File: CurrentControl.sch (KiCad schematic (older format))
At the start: 7 parts

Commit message: Initial annotation
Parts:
- Q201: renamed from Q?; footprint (none) -> Transistors_TO-220:TO-220_FET-GDS_Vertical
- R201, R202: renamed from R?; footprint (none) -> Resistors_SMD:R_0603_HandSoldering
- R203: renamed from R?; footprint (none) -> Resistors_ThroughHole:Resistor_Vertical_RM5mm
- U201: renamed from U?; footprint (none) -> SMD_Packages:SSOP-8
- gave numbers to parts that had none: 2
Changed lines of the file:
@@
 $EndDescr
 $Comp
-L R R?
+L R R202
 U 1 1 54E39380
 P 3200 3800
-F 0 "R?" V 3280 3800 50  0000 C CNN
+F 0 "R202" V 3280 3800 50  0000 C CNN
 F 1 "R" V 3207 3801 50  0000 C CNN
-F 2 "" V 3130 3800 30  0000 C CNN
+F 2 "Resistors_SMD:R_0603_HandSoldering" V 3130 3800 30  0001 C CNN
 F 3 "" H 3200 3800 30  0000 C CNN
 	1    3200 3800
@@
 $EndComp
 $Comp
-L R R?
+L R R203
 U 1 1 54E39388
 P 6650 4350
-F 0 "R?" V 6730 4350 50  0000 C CNN
+F 0 "R203" V 6730 4350 50  0000 C CNN
 F 1 ".1" V 6657 4351 50  0000 C CNN
-F 2 "" V 6580 4350 30  0000 C CNN
+F 2 "Resistors_ThroughHole:Resistor_Vertical_RM5mm" V 6580 4350 30  0001 C CNN
 F 3 "" H 6650 4350 30  0000 C CNN
 F 4 "AC01000001007JA100" V 6650 4350 60  0001 C CNN "MPN"
@@
 $EndComp
 $Comp
-L LMV358 U?
+L LMV358 U201
 U 1 1 54E3939B
 P 4550 3000
-F 0 "U?" H 4500 3200 60  0000 L CNN
+F 0 "U201" H 4500 3200 60  0000 L CNN
 F 1 "LMV358" H 4500 2750 60  0000 L CNN
-F 2 "" H 4550 3000 60  0000 C CNN
+F 2 "SMD_Packages:SSOP-8" H 4550 3000 60  0001 C CNN
 F 3 "" H 4550 3000 60  0000 C CNN
 	1    4550 3000
@@
 $EndComp
 $Comp
-L MOSFET_N Q?
+L MOSFET_N Q201
 U 1 1 54E393A3
 P 6550 3000
-F 0 "Q?" H 6560 3170 50  0000 R CNN
+F 0 "Q201" H 6560 3170 50  0000 R CNN
 F 1 "BUK9575" H 6500 2850 50  0000 R CNN
-F 2 "" H 6550 3000 60  0000 C CNN
+F 2 "Transistors_TO-220:TO-220_FET-GDS_Vertical" H 6550 3000 60  0001 C CNN
 F 3 "" H 6550 3000 60  0000 C CNN
 F 4 "BUK9575-100A,127" H 6550 3000 60  0001 C CNN "MPN"
@@
 $EndComp
 $Comp
-L C C?
+L C C201
 U 1 1 54E393B0
 P 4050 2300
-F 0 "C?" H 4100 2400 50  0000 L CNN
+F 0 "C201" H 4100 2400 50  0000 L CNN
 F 1 "C" H 4100 2200 50  0000 L CNN
-F 2 "" H 4088 2150 30  0000 C CNN
+F 2 "" H 4088 2150 30  0001 C CNN
 F 3 "" H 4050 2300 60  0000 C CNN
 	1    4050 2300
@@
 	3850 3100 3850 3950
 $Comp
-L POT RV?
+L POT RV201
 U 1 1 54E393C3
 P 3200 3100
-F 0 "RV?" H 3200 3000 50  0000 C CNN
+F 0 "RV201" H 3200 3000 50  0000 C CNN
 F 1 "POT" H 3200 3100 50  0000 C CNN
-F 2 "" H 3200 3100 60  0000 C CNN
+F 2 "" H 3200 3100 60  0001 C CNN
 F 3 "" H 3200 3100 60  0000 C CNN
 	1    3200 3100
@@
 	6650 2000 6650 2800
 $Comp
-L R R?
+L R R201
 U 1 1 54E39622
 P 5650 3000
-F 0 "R?" V 5730 3000 50  0000 C CNN
+F 0 "R201" V 5730 3000 50  0000 C CNN
 F 1 "1K" V 5657 3001 50  0000 C CNN
-F 2 "" V 5580 3000 30  0000 C CNN
+F 2 "Resistors_SMD:R_0603_HandSoldering" V 5580 3000 30  0001 C CNN
 F 3 "" H 5650 3000 30  0000 C CNN
 	1    5650 3000

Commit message: Preliminary footprint association
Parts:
- C201: footprint (none) -> SMD_Packages:SMD-0805
- R201, R202: footprint Resistors_SMD:R_0603_HandSoldering -> SMD_Packages:SMD-0805
- R203: footprint Resistors_ThroughHole:Resistor_Vertical_RM5mm -> Resistors_ThroughHole:Resistor_Horizontal_RM15mm
- RV201: footprint (none) -> Potentiometers:Potentiometer_WirePads_largePads
- U201: footprint SMD_Packages:SSOP-8 -> SMD_Packages:SOIC-8-N; MPN (none) -> LMV358IDT
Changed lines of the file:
@@
 F 0 "R202" V 3280 3800 50  0000 C CNN
 F 1 "R" V 3207 3801 50  0000 C CNN
-F 2 "Resistors_SMD:R_0603_HandSoldering" V 3130 3800 30  0001 C CNN
+F 2 "SMD_Packages:SMD-0805" V 3130 3800 30  0001 C CNN
 F 3 "" H 3200 3800 30  0000 C CNN
 	1    3200 3800
@@
 F 0 "R203" V 6730 4350 50  0000 C CNN
 F 1 ".1" V 6657 4351 50  0000 C CNN
-F 2 "Resistors_ThroughHole:Resistor_Vertical_RM5mm" V 6580 4350 30  0001 C CNN
+F 2 "Resistors_ThroughHole:Resistor_Horizontal_RM15mm" V 6580 4350 30  0001 C CNN
 F 3 "" H 6650 4350 30  0000 C CNN
 F 4 "AC01000001007JA100" V 6650 4350 60  0001 C CNN "MPN"
@@
 F 0 "U201" H 4500 3200 60  0000 L CNN
 F 1 "LMV358" H 4500 2750 60  0000 L CNN
-F 2 "SMD_Packages:SSOP-8" H 4550 3000 60  0001 C CNN
-F 3 "" H 4550 3000 60  0000 C CNN
+F 2 "SMD_Packages:SOIC-8-N" H 4550 3000 60  0001 C CNN
+F 3 "http://www.produktinfo.conrad.com/datenblaetter/1100000-1199999/001185383-da-01-en-IC_OP_AMP_DUAL_R_R_LMV358IDT_SOIC_8_STM.pdf" H 4550 3000 60  0001 C CNN
+F 4 "LMV358IDT" H 4550 3000 60  0001 C CNN "MPN"
 	1    4550 3000
 	1    0    0    -1
@@
 F 0 "C201" H 4100 2400 50  0000 L CNN
 F 1 "C" H 4100 2200 50  0000 L CNN
-F 2 "" H 4088 2150 30  0001 C CNN
+F 2 "SMD_Packages:SMD-0805" H 4088 2150 30  0001 C CNN
 F 3 "" H 4050 2300 60  0000 C CNN
 	1    4050 2300
@@
 F 0 "RV201" H 3200 3000 50  0000 C CNN
 F 1 "POT" H 3200 3100 50  0000 C CNN
-F 2 "" H 3200 3100 60  0001 C CNN
+F 2 "Potentiometers:Potentiometer_WirePads_largePads" H 3200 3100 60  0001 C CNN
 F 3 "" H 3200 3100 60  0000 C CNN
 	1    3200 3100
@@
 F 0 "R201" V 5730 3000 50  0000 C CNN
 F 1 "1K" V 5657 3001 50  0000 C CNN
-F 2 "Resistors_SMD:R_0603_HandSoldering" V 5580 3000 30  0001 C CNN
+F 2 "SMD_Packages:SMD-0805" V 5580 3000 30  0001 C CNN
 F 3 "" H 5650 3000 30  0000 C CNN
 	1    5650 3000

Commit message: Rough board layout
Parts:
- added P201: CONN_01X01, CSOS Local:FA-220-38E, symbol CONN_01X01
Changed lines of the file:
@@
 Text HLabel 7250 4600 2    60   Input ~ 0
 Current_Sink-
+$Comp
+L CONN_01X01 P201
+U 1 1 54E78AC3
+P 7300 3000
+F 0 "P201" H 7300 3100 50  0000 C CNN
+F 1 "CONN_01X01" V 7400 3000 50  0000 C CNN
+F 2 "CSOS Local:FA-220-38E" H 7300 3000 60  0001 C CNN
+F 3 "" H 7300 3000 60  0000 C CNN
+	1    7300 3000
+	1    0    0    -1
+$EndComp
 $EndSCHEMATC

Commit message: Updated the POT references and schematic
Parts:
- R202: value R -> 68K; MPN (none) -> Value
- RV201: value POT -> 10K; footprint Potentiometers:Potentiometer_WirePads_largePads -> CSOS Local:P090L-02F25BR10K; MPN (none) -> Value
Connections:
- wire segments 23 -> 22
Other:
- moved on the sheet: R202, RV201
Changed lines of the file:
@@
 L R R202
 U 1 1 54E39380
-P 3200 3800
-F 0 "R202" V 3280 3800 50  0000 C CNN
-F 1 "R" V 3207 3801 50  0000 C CNN
-F 2 "SMD_Packages:SMD-0805" V 3130 3800 30  0001 C CNN
-F 3 "" H 3200 3800 30  0000 C CNN
-	1    3200 3800
+P 3200 3100
+F 0 "R202" V 3280 3100 50  0000 C CNN
+F 1 "68K" V 3207 3101 50  0000 C CNN
+F 2 "SMD_Packages:SMD-0805" V 3130 3100 30  0001 C CNN
+F 3 "" H 3200 3100 30  0000 C CNN
+F 4 "Value" H 3200 3100 60  0001 C CNN "MPN"
+	1    3200 3100
 	1    0    0    -1
 $EndComp
@@
 	6650 3200 6650 4100
 Wire Wire Line
+	3200 3350 3650 3350
+Wire Wire Line
 	3200 3350 3200 3550
-Wire Wire Line
-	3200 4050 3200 4600
 Wire Wire Line
 	3850 3950 6650 3950
@@
 L POT RV201
 U 1 1 54E393C3
-P 3200 3100
-F 0 "RV201" H 3200 3000 50  0000 C CNN
-F 1 "POT" H 3200 3100 50  0000 C CNN
-F 2 "Potentiometers:Potentiometer_WirePads_largePads" H 3200 3100 60  0001 C CNN
-F 3 "" H 3200 3100 60  0000 C CNN
-	1    3200 3100
+P 3200 3800
+F 0 "RV201" H 3200 3700 50  0000 C CNN
+F 1 "10K" H 3200 3800 50  0000 C CNN
+F 2 "CSOS Local:P090L-02F25BR10K" H 3200 3800 60  0001 C CNN
+F 3 "" H 3200 3800 60  0000 C CNN
+F 4 "Value" H 3200 3800 60  0001 C CNN "MPN"
+	1    3200 3800
 	0    1    1    0
 $EndComp
 Wire Wire Line
-	3450 3100 3350 3100
-Wire Wire Line
-	3450 2000 3450 3100
+	3200 2000 3200 2850
 Wire Wire Line
 	4450 2000 4450 2600
 Wire Wire Line
 	2950 2000 4450 2000
-Connection ~ 3450 2000
+Connection ~ 3200 2000
 Wire Wire Line
 	4050 2100 4050 2000
@@
 	4050 2900 3650 2900
 Wire Wire Line
-	3650 2900 3650 3450
-Wire Wire Line
-	3650 3450 3200 3450
-Connection ~ 3200 3450
+	3650 2900 3650 3350
 Text GLabel 2950 2000 0    60   Input ~ 0
 2.7V
@@
 FET_GATE
 Wire Wire Line
-	3200 4600 7250 4600
+	3350 4600 7250 4600
 Connection ~ 6650 4600
 Text HLabel 7250 4600 2    60   Input ~ 0
@@
 P 7300 3000
 F 0 "P201" H 7300 3100 50  0000 C CNN
-F 1 "CONN_01X01" V 7400 3000 50  0000 C CNN
+F 1 "CONN_01X01" V 7400 3000 50  0001 C CNN
 F 2 "CSOS Local:FA-220-38E" H 7300 3000 60  0001 C CNN
 F 3 "" H 7300 3000 60  0000 C CNN
@@
 	1    0    0    -1
 $EndComp
+Wire Wire Line
+	3350 4600 3350 3800
 $EndSCHEMATC

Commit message: First cut of layout in preperation for the final session
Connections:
- no-connect marks 0 -> 3
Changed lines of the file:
@@
 Connection ~ 6650 3950
-Wire Wire Line
-	4450 3400 4450 3500
 Wire Wire Line
 	4050 3100 3850 3100
@@
 FET_GATE
 Wire Wire Line
-	3350 4600 7250 4600
+	3350 4600 7300 4600
 Connection ~ 6650 4600
-Text HLabel 7250 4600 2    60   Input ~ 0
+Text HLabel 7300 4600 2    60   Input ~ 0
 Current_Sink-
 $Comp
@@
 Wire Wire Line
 	3350 4600 3350 3800
+NoConn ~ 7100 3000
+NoConn ~ 3200 4050
+NoConn ~ 1800 1650
+Wire Wire Line
+	4450 3400 4450 3500
 $EndSCHEMATC

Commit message: Routing and fixing schematic checkpoint
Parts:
- R203: footprint Resistors_ThroughHole:Resistor_Horizontal_RM15mm -> Resistors_ThroughHole:Resistor_Vertical_RM5mm
- U201: footprint SMD_Packages:SOIC-8-N -> (none); MPN LMV358IDT -> (none)
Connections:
- wire segments 22 -> 27
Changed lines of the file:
@@
 F 0 "R203" V 6730 4350 50  0000 C CNN
 F 1 ".1" V 6657 4351 50  0000 C CNN
-F 2 "Resistors_ThroughHole:Resistor_Horizontal_RM15mm" V 6580 4350 30  0001 C CNN
+F 2 "Resistors_ThroughHole:Resistor_Vertical_RM5mm" V 6580 4350 30  0001 C CNN
 F 3 "" H 6650 4350 30  0000 C CNN
 F 4 "AC01000001007JA100" V 6650 4350 60  0001 C CNN "MPN"
 	1    6650 4350
-	1    0    0    -1
-$EndComp
-$Comp
-L LMV358 U201
-U 1 1 54E3939B
-P 4550 3000
-F 0 "U201" H 4500 3200 60  0000 L CNN
-F 1 "LMV358" H 4500 2750 60  0000 L CNN
-F 2 "SMD_Packages:SOIC-8-N" H 4550 3000 60  0001 C CNN
-F 3 "http://www.produktinfo.conrad.com/datenblaetter/1100000-1199999/001185383-da-01-en-IC_OP_AMP_DUAL_R_R_LMV358IDT_SOIC_8_STM.pdf" H 4550 3000 60  0001 C CNN
-F 4 "LMV358IDT" H 4550 3000 60  0001 C CNN "MPN"
-	1    4550 3000
 	1    0    0    -1
 $EndComp
@@
 $EndComp
 $Comp
-L GND #PWR03
+L GND #PWR202
 U 1 1 54E393AA
 P 4450 3500
-F 0 "#PWR03" H 4450 3250 60  0001 C CNN
+F 0 "#PWR202" H 4450 3250 60  0001 C CNN
 F 1 "GND" H 4450 3350 60  0000 C CNN
 F 2 "" H 4450 3500 60  0000 C CNN
@@
 $EndComp
 Wire Wire Line
-	6650 3200 6650 4100
+	6650 3200 6650 3950
+Wire Wire Line
+	6650 3950 6650 4100
 Wire Wire Line
 	3200 3350 3650 3350
@@
 	4450 2000 4450 2600
 Wire Wire Line
-	2950 2000 4450 2000
+	2950 2000 3200 2000
+Wire Wire Line
+	3200 2000 4050 2000
+Wire Wire Line
+	4050 2000 4450 2000
 Connection ~ 3200 2000
 Wire Wire Line
@@
 Connection ~ 4050 2000
 $Comp
-L GND #PWR04
+L GND #PWR201
 U 1 1 54E393D3
 P 4050 2600
-F 0 "#PWR04" H 4050 2350 60  0001 C CNN
+F 0 "#PWR201" H 4050 2350 60  0001 C CNN
 F 1 "GND" H 4050 2450 60  0000 C CNN
 F 2 "" H 4050 2600 60  0000 C CNN
@@
 	5050 3000 5400 3000
 Wire Wire Line
-	5900 3000 6350 3000
+	5900 3000 6100 3000
+Wire Wire Line
+	6100 3000 6350 3000
 Wire Wire Line
 	6100 3000 6100 1650
@@
 FET_GATE
 Wire Wire Line
-	3350 4600 7300 4600
+	3350 4600 6650 4600
+Wire Wire Line
+	6650 4600 7300 4600
 Connection ~ 6650 4600
 Text HLabel 7300 4600 2    60   Input ~ 0
@@
 Wire Wire Line
 	4450 3400 4450 3500
+$Comp
+L LMV358 U201
+U 1 1 54F4A8C6
+P 4550 3000
+F 0 "U201" H 4500 3200 60  0000 L CNN
+F 1 "LMV358" H 4500 2750 60  0000 L CNN
+F 2 "" H 4550 3000 60  0000 C CNN
+F 3 "" H 4550 3000 60  0000 C CNN
+	1    4550 3000
+	1    0    0    -1
+$EndComp
 $EndSCHEMATC

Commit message: Initial route before filling the ground plane
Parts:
- removed U201: LMV358, symbol LMV358
- added U201: LMV358, symbol LMV358
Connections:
- wire segments 27 -> 22
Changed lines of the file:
@@
 $EndComp
 $Comp
-L GND #PWR202
+L GND #PWR03
 U 1 1 54E393AA
 P 4450 3500
-F 0 "#PWR202" H 4450 3250 60  0001 C CNN
+F 0 "#PWR03" H 4450 3250 60  0001 C CNN
 F 1 "GND" H 4450 3350 60  0000 C CNN
 F 2 "" H 4450 3500 60  0000 C CNN
@@
 $EndComp
 Wire Wire Line
-	6650 3200 6650 3950
-Wire Wire Line
-	6650 3950 6650 4100
+	6650 3200 6650 4100
 Wire Wire Line
 	3200 3350 3650 3350
@@
 	4450 2000 4450 2600
 Wire Wire Line
-	2950 2000 3200 2000
-Wire Wire Line
-	3200 2000 4050 2000
-Wire Wire Line
-	4050 2000 4450 2000
+	2950 2000 4450 2000
 Connection ~ 3200 2000
 Wire Wire Line
@@
 Connection ~ 4050 2000
 $Comp
-L GND #PWR201
+L GND #PWR04
 U 1 1 54E393D3
 P 4050 2600
-F 0 "#PWR201" H 4050 2350 60  0001 C CNN
+F 0 "#PWR04" H 4050 2350 60  0001 C CNN
 F 1 "GND" H 4050 2450 60  0000 C CNN
 F 2 "" H 4050 2600 60  0000 C CNN
@@
 	5050 3000 5400 3000
 Wire Wire Line
-	5900 3000 6100 3000
-Wire Wire Line
-	6100 3000 6350 3000
+	5900 3000 6350 3000
 Wire Wire Line
 	6100 3000 6100 1650
@@
 FET_GATE
 Wire Wire Line
-	3350 4600 6650 4600
-Wire Wire Line
-	6650 4600 7300 4600
+	3350 4600 7300 4600
 Connection ~ 6650 4600
 Text HLabel 7300 4600 2    60   Input ~ 0
@@
 $Comp
 L LMV358 U201
-U 1 1 54F4A8C6
+U 2 1 54F4B111
 P 4550 3000
 F 0 "U201" H 4500 3200 60  0000 L CNN
@@
 F 2 "" H 4550 3000 60  0000 C CNN
 F 3 "" H 4550 3000 60  0000 C CNN
-	1    4550 3000
+F 4 "Value" H 4550 3000 60  0001 C CNN "MPN"
+	2    4550 3000
 	1    0    0    -1
 $EndComp

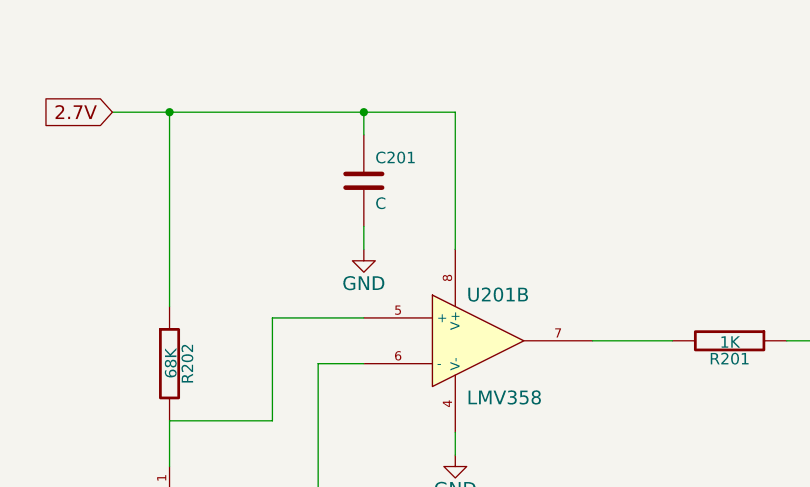
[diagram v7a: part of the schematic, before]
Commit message: Final update to BOM and added the bom XSL script
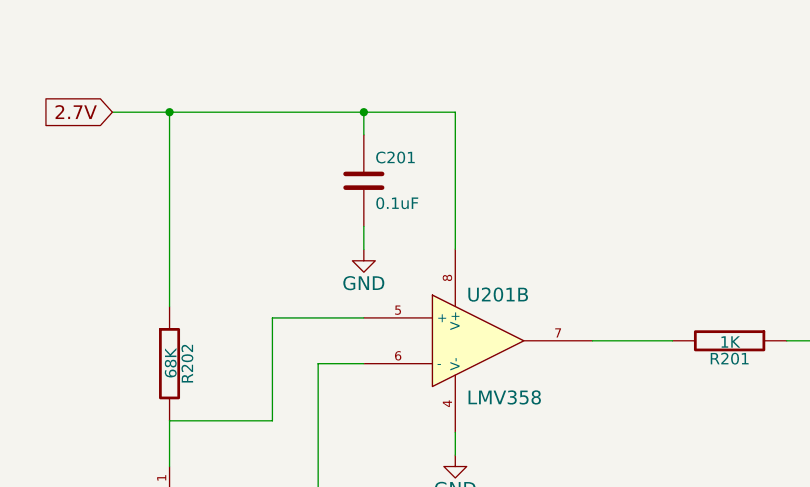
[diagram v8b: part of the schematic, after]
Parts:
- C201: value C -> 0.1uF
- P201: value CONN_01X01 -> HEATSINK; MPN (none) -> FA-T220-38E
- R202: MPN Value -> (none)
- RV201: MPN Value -> P090L-02F25BR10K
- U201: MPN Value -> LMV358IDT
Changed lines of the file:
@@
 F 2 "SMD_Packages:SMD-0805" V 3130 3100 30  0001 C CNN
 F 3 "" H 3200 3100 30  0000 C CNN
-F 4 "Value" H 3200 3100 60  0001 C CNN "MPN"
 	1    3200 3100
 	1    0    0    -1
@@
 P 4050 2300
 F 0 "C201" H 4100 2400 50  0000 L CNN
-F 1 "C" H 4100 2200 50  0000 L CNN
+F 1 "0.1uF" H 4100 2200 50  0000 L CNN
 F 2 "SMD_Packages:SMD-0805" H 4088 2150 30  0001 C CNN
 F 3 "" H 4050 2300 60  0000 C CNN
@@
 F 2 "CSOS Local:P090L-02F25BR10K" H 3200 3800 60  0001 C CNN
 F 3 "" H 3200 3800 60  0000 C CNN
-F 4 "Value" H 3200 3800 60  0001 C CNN "MPN"
+F 4 "P090L-02F25BR10K" H 3200 3800 60  0001 C CNN "MPN"
 	1    3200 3800
 	0    1    1    0
@@
 P 7300 3000
 F 0 "P201" H 7300 3100 50  0000 C CNN
-F 1 "CONN_01X01" V 7400 3000 50  0001 C CNN
+F 1 "HEATSINK" V 7400 3000 50  0001 C CNN
 F 2 "CSOS Local:FA-220-38E" H 7300 3000 60  0001 C CNN
 F 3 "" H 7300 3000 60  0000 C CNN
+F 4 "FA-T220-38E" H 7300 3000 60  0001 C CNN "MPN"
 	1    7300 3000
 	1    0    0    -1
@@
 F 2 "" H 4550 3000 60  0000 C CNN
 F 3 "" H 4550 3000 60  0000 C CNN
-F 4 "Value" H 4550 3000 60  0001 C CNN "MPN"
+F 4 "LMV358IDT" H 4550 3000 60  0001 C CNN "MPN"
 	2    4550 3000
 	1    0    0    -1
